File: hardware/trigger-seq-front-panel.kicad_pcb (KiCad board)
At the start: 2 copper layers, 81.3 x 128.5 mm, 57 parts

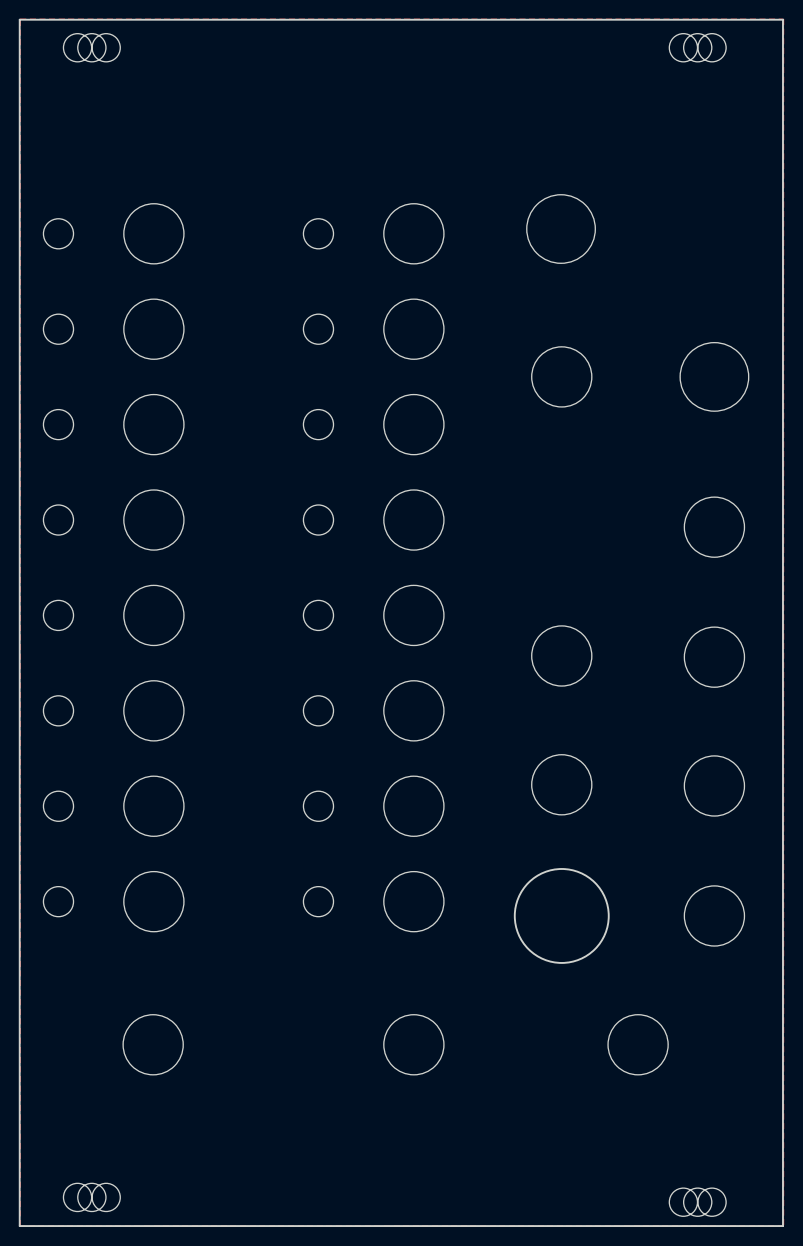
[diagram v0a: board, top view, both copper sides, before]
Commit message: replaced old hardware files with the most recent ones tracking CLAUDE.md AI files used in revising the project
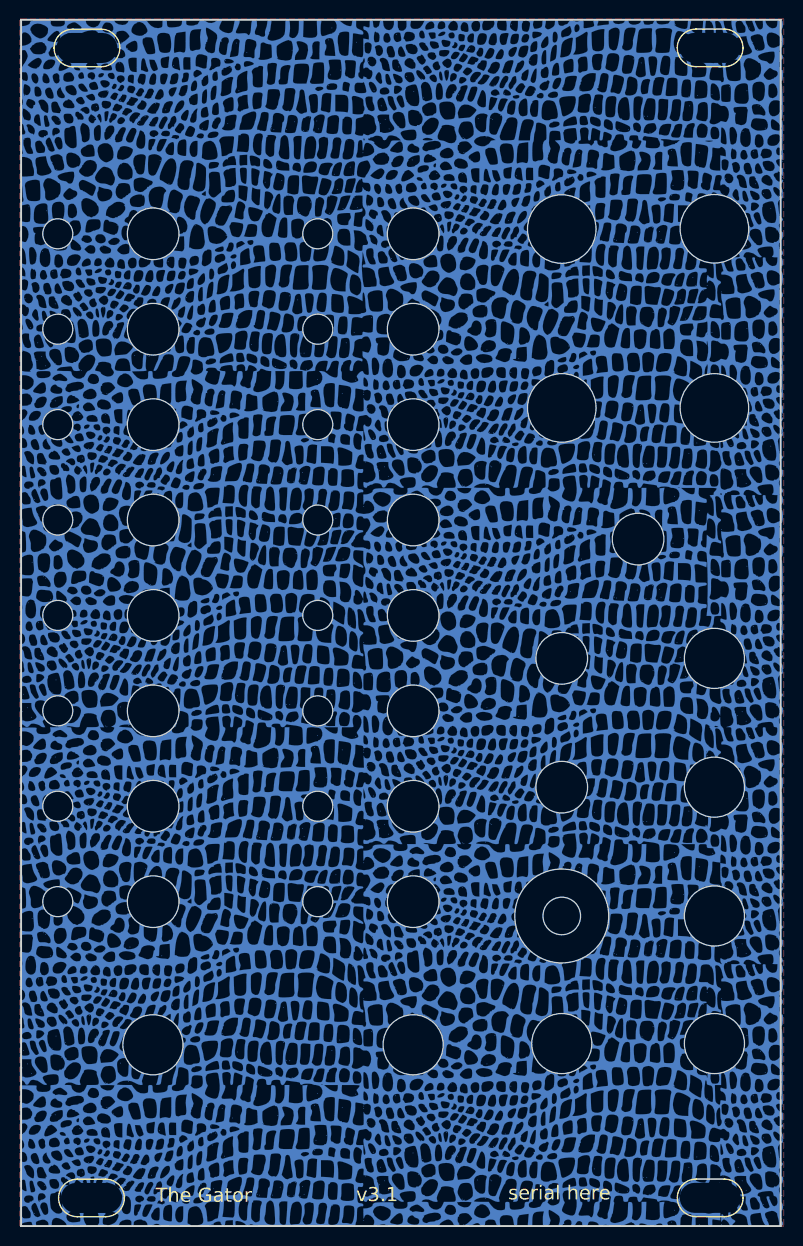
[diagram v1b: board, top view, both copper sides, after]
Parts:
- removed the REF** at (143.3, 44.2)
- removed the REF** at (81.8, 166.6)
- removed the REF** at (78.7, 166.6)
- removed the REF** at (86.8, 150.4)
- removed the REF** at (138.4, 150.4)
- removed the REF** at (146.6, 122.8)
- removed the REF** at (146.6, 109.1)
- removed the REF** at (146.6, 95.2)
- removed the REF** at (146.3, 44.2)
- removed the REF** at (130.3, 122.7)
- removed the REF** at (114.6, 135.1)
- removed the REF** at (114.6, 125.0)
- removed the REF** at (130.3, 79.2)
- removed the REF** at (130.3, 109.0)
- removed the REF** at (114.6, 114.8)
- removed the REF** at (114.6, 104.6)
- removed the REF** at (114.6, 94.5)
- removed the REF** at (114.6, 84.3)
- removed the REF** at (114.6, 74.2)
- removed the REF** at (144.8, 44.2)
- removed the REF** at (114.6, 64.0)
- removed the REF** at (86.9, 135.1)
- removed the REF** at (86.9, 125.0)
- removed the REF** at (86.9, 114.8)
- removed the REF** at (86.9, 104.6)
- removed the REF** at (86.9, 94.5)
- removed the REF** at (86.9, 84.3)
- removed the REF** at (86.9, 74.2)
- removed the REF** at (86.9, 64.0)
- removed the REF** at (146.3, 167.1)
- removed the REF** at (104.4, 135.1)
- removed the REF** at (76.7, 135.1)
- removed the REF** at (143.3, 167.1)
- removed the REF** at (76.7, 74.2)
- removed the REF** at (130.2, 63.5)
- removed the REF** at (80.3, 166.6)
- removed the REF** at (144.8, 167.1)
- removed the REF** at (81.8, 44.2)
- removed the REF** at (78.7, 44.2)
- removed the REF** at (80.3, 44.2)
- added G***: LOGO, My Library:gator-inverse-back-copper, B.Cu at (113.2, 105.5)
- added REF**: MountingHole_5.5mm, MountingHole:MountingHole_5.5mm, F.Cu at (130.3, 122.9)
- added REF**: MountingHole_5.5mm, MountingHole:MountingHole_5.5mm, F.Cu at (130.3, 109.2)
- added REF**: MountingHole_7.3mm, Mounting_Holes:MountingHole_7.3mm, F.Cu at (130.3, 63.5)
- added REF**: MountingHole_5.5mm, MountingHole:MountingHole_5.5mm, F.Cu at (114.5, 135.1)
- added REF**: MountingHole_5.5mm, MountingHole:MountingHole_5.5mm, F.Cu at (114.5, 125.0)
- added REF**: MountingHole_5.5mm, MountingHole:MountingHole_5.5mm, F.Cu at (114.5, 114.8)
- added REF**: MountingHole_5.5mm, MountingHole:MountingHole_5.5mm, F.Cu at (114.5, 104.6)
- added REF**: MountingHole_5.5mm, MountingHole:MountingHole_5.5mm, F.Cu at (114.5, 94.5)
- added REF**: EuroMountingSlot, My Library:EuroMountingSlot, F.Cu at (80.2, 166.7)
- added REF**: EuroMountingSlot, My Library:EuroMountingSlot, F.Cu at (146.1, 166.7)
- added REF**: MountingHole_5.5mm, MountingHole:MountingHole_5.5mm, F.Cu at (114.5, 84.3)
- added REF**: MountingHole_5.5mm, MountingHole:MountingHole_5.5mm, F.Cu at (114.5, 74.2)
- added REF**: EuroMountingSlot, My Library:EuroMountingSlot, F.Cu at (146.1, 44.2)
- added REF**: MountingHole_5.5mm, MountingHole:MountingHole_5.5mm, F.Cu at (114.5, 64.0)
- added REF**: EuroMountingSlot, My Library:EuroMountingSlot, F.Cu at (79.7, 44.2)
- added REF**: MountingHole_5.5mm, MountingHole:MountingHole_5.5mm, F.Cu at (86.8, 125.0)
- added REF**: MountingHole_5.5mm, MountingHole:MountingHole_5.5mm, F.Cu at (86.8, 114.8)
- added REF**: MountingHole_5.5mm, MountingHole:MountingHole_5.5mm, F.Cu at (86.8, 104.6)
- added REF**: MountingHole_5.5mm, MountingHole:MountingHole_5.5mm, F.Cu at (86.8, 94.5)
- added REF**: MountingHole_5.5mm, MountingHole:MountingHole_5.5mm, F.Cu at (86.8, 84.3)
- added REF**: MountingHole_5.5mm, MountingHole:MountingHole_5.5mm, F.Cu at (86.8, 74.2)
- added REF**: MountingHole_5.5mm, MountingHole:MountingHole_5.5mm, F.Cu at (86.8, 64.0)
- added REF**: MountingHole_3.2mm_M3, Mounting_Holes:MountingHole_3.2mm_M3, F.Cu at (76.6, 74.2)
- added REF**: MountingHole_5.5mm, MountingHole:MountingHole_5.5mm, F.Cu at (86.8, 135.1)
- added REF**: MountingHole_3.2mm_M3, Mounting_Holes:MountingHole_3.2mm_M3, F.Cu at (76.6, 135.1)
- added REF**: MountingHole_3.2mm_M3, Mounting_Holes:MountingHole_3.2mm_M3, F.Cu at (104.3, 135.1)
- added REF**: MountingHole_6.4mm_M6, Mounting_Holes:MountingHole_6.4mm_M6, F.Cu at (86.8, 150.4)
- added REF**: MountingHole_6.4mm_M6, Mounting_Holes:MountingHole_6.4mm_M6, F.Cu at (130.3, 150.2)
- added REF**: MountingHole_6.4mm_M6, Mounting_Holes:MountingHole_6.4mm_M6, F.Cu at (146.6, 150.2)
- added REF**: MountingHole_10mm_dia, My Library:MountingHole_10mm_dia, F.Cu at (130.3, 136.7)
- added REF**: MountingHole_6.4mm_M6, Mounting_Holes:MountingHole_6.4mm_M6, F.Cu at (146.6, 122.9)
- added REF**: MountingHole_6.4mm_M6, Mounting_Holes:MountingHole_6.4mm_M6, F.Cu at (146.6, 109.2)
- added REF**: MountingHole_5.5mm, MountingHole:MountingHole_5.5mm, F.Cu at (138.4, 96.5)
- added REF**: MountingHole_7.3mm, Mounting_Holes:MountingHole_7.3mm, F.Cu at (130.3, 82.5)
- added REF**: MountingHole_7.3mm, Mounting_Holes:MountingHole_7.3mm, F.Cu at (146.6, 82.5)
- moved G*** 108.4 mm to (101.0, 161.4)
- moved REF** 15.8 mm to (146.6, 63.5)
- moved REF** 0.08 mm to (114.5, 150.4)
- moved REF** 0.08 mm to (104.3, 104.6)
- moved REF** 0.08 mm to (104.3, 94.5)
- moved REF** 0.08 mm to (104.3, 84.3)
- moved REF** 0.08 mm to (104.3, 74.2)
- moved REF** 0.08 mm to (104.3, 64.0)
- moved REF** 0.08 mm to (76.6, 64.0)
- moved REF** 0.08 mm to (76.6, 84.3)
- moved REF** 0.08 mm to (76.6, 94.5)
- moved REF** 0.08 mm to (76.6, 104.6)
- moved REF** 0.08 mm to (76.6, 114.8)
- moved REF** 0.08 mm to (76.6, 125.0)
- moved REF** 0.08 mm to (104.3, 125.0)
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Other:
- board size 81.3 x 128.5 mm -> 80.9 x 128.5 mm
- net class Default removed
- net class power removed
- board text added: "The Gator"
- board text added: "The Gator Trigger Sequencer"
- board text added: "back"
- board text added: "fwd"
- board text added: "serial here"
- board text added: "steps"
- board text added: "swing"
- board text added: "v3.1"
- board text removed: "Frogleg Synthesis"
- board text removed: "Hook's Gator Trigger Sequencer"
- board text removed: "down"
- board text removed: "up"
